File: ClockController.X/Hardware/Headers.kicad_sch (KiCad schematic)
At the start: 6 parts, among them Q5 MMBT2222A-TP, Q6 MMBT2222A-TP

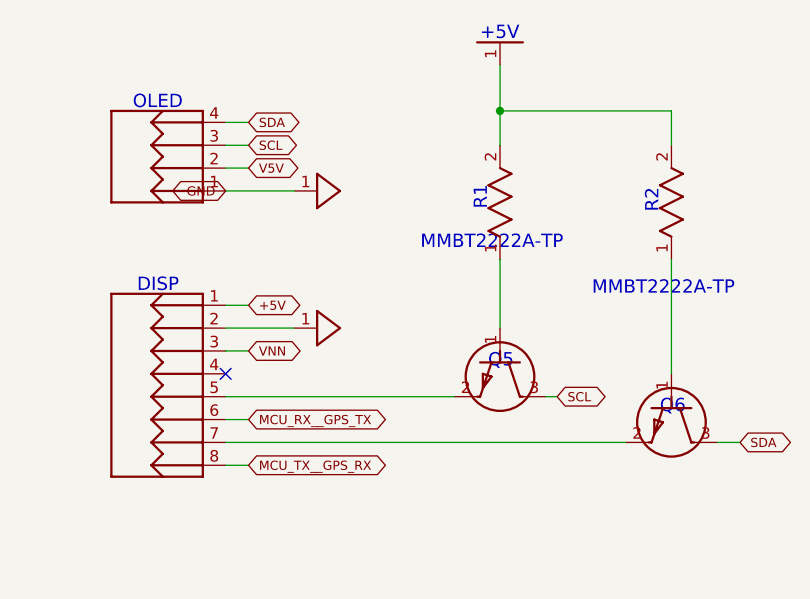
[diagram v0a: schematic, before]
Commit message: Replace the imported objects with native kicad equivalents
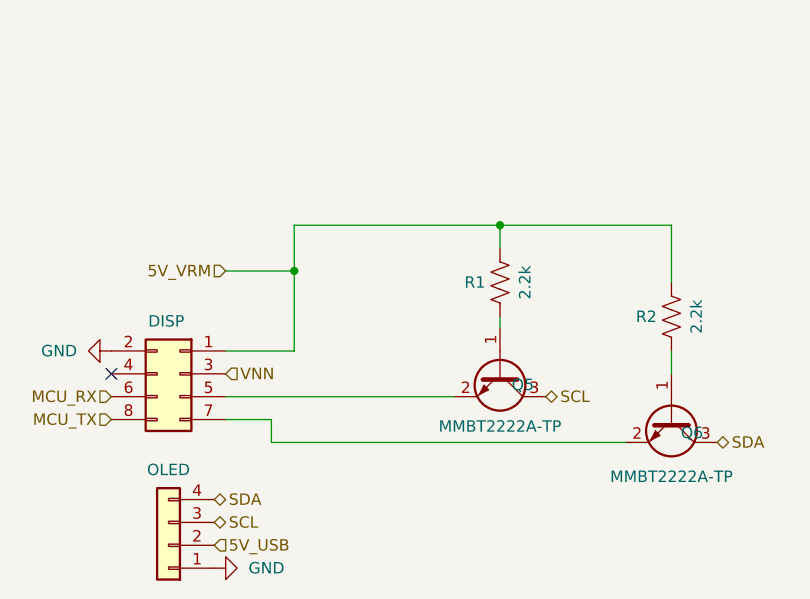
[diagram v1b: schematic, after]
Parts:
- DISP0: value HDR-2X4 -> DISP; symbol Clock Controller-eagle-import:HDR-2X4 -> Connector_Generic:Conn_02x04_Odd_Even
- OLED0: value HDR-1X4 -> OLED; symbol Clock Controller-eagle-import:HDR-1X4 -> Connector_Generic:Conn_01x04
- Q5, Q6: symbol Clock Controller-eagle-import:MMBT2222A-TP -> Transistor_BJT:MMBT2222A
- R1, R2: symbol Clock Controller-eagle-import:RES_1206 -> Device:R_US
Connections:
- net GND_DIGITAL_3 is gone; now on net GND: OLED0.1 (Pin_1)
- net +5V renamed 5V_VRM
- net GND_DIGITAL renamed GND
- net MCU_RX__GPS_TX renamed MCU_RX
- net MCU_TX__GPS_RX renamed MCU_TX
- net V5V renamed 5V_USB
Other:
- note removed: "+5V"
- note removed: "DISP"
- note removed: "MMBT2222A-TP"
- note removed: "OLED"
- note removed: "Q5"
- note removed: "Q6"
- note removed: "R1"
- note removed: "R2"
